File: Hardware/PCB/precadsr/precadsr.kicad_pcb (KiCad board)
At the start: 2 copper layers, 114 x 180 mm, 80 parts, among them J1 AudioJack2_SwitchT, J12 AudioJack2, J13 AudioJack2, J2 Synth_power_2x5, J3 2_pin_Molex_header, J4 Conn_01x10, J5 AudioJack2, J6 Conn_01x04, J7 Conn_01x10, J8 Conn_01x04, J9 2_pin_Molex_connector, Q1 2N3904, Q2 2N3904, Q3 2N3904, U1 ICM7555xP, U2 TL074, U3 LM358

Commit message: Various tweaks
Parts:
- C1, C11: value 1 nF -> 1nF
- C10: value 1 uF -> 1uF
- C2: value 10 nF -> 10nF
- C3: value 10 uF -> 10uF; footprint ao_tht:CP_Radial_D5.0mm_P2.00mm -> ao_tht:CP_Radial_D6.3mm_P2.50mm
- C6, C7, C8, C9: value 100 nF -> 100nF
- moved C3 4.02 mm to (101.6, 27.9), turned to 180 degrees
- moved C10 2.50 mm to (88.9, 27.9), turned to 0 degrees
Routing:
- net SPEED_3: track 7.57 -> 5.16 mm
- net SPEED_1: track 7.30 -> 5.81 mm
- net GATE: track 114.6 -> 113.5 mm
- net THR: track 130.5 -> 131.3 mm

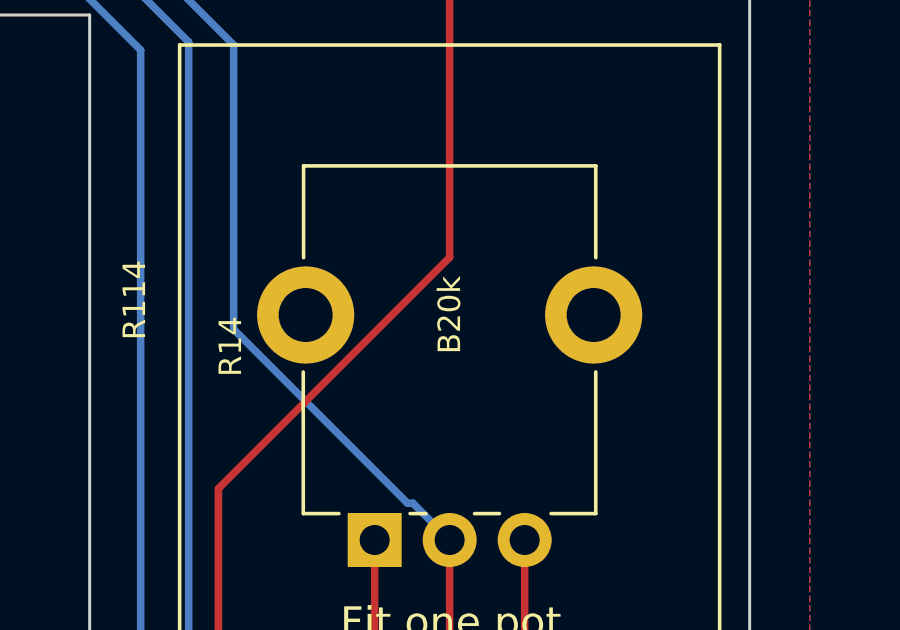
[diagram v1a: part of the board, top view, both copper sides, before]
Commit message: Add comments and graphics symbols to schematics
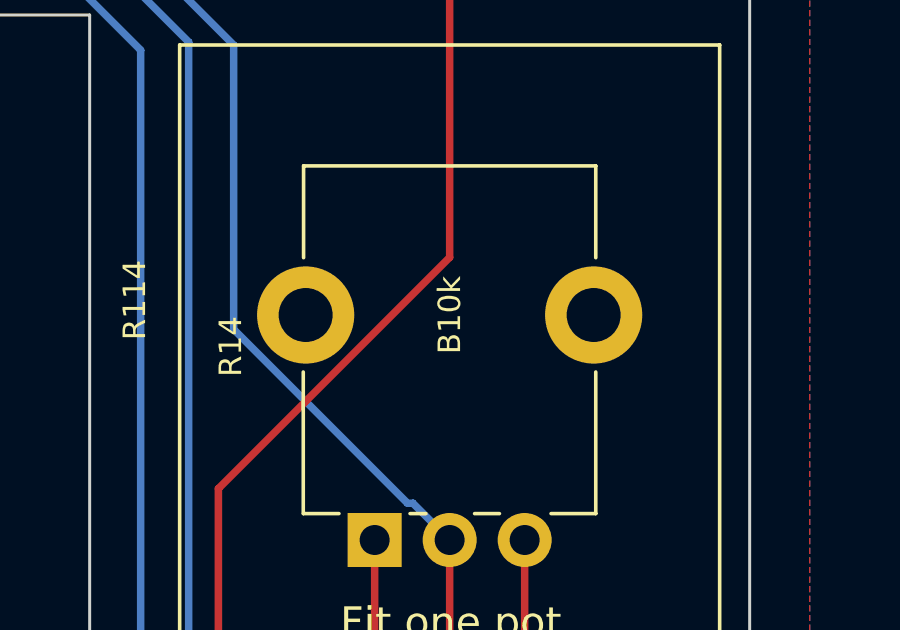
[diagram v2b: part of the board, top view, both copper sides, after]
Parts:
- removed G*** (x2): LOGO, precadsr-panel:precadsr-panel-holes
- added GRAF1: Panel holes, precadsr-panel:precadsr-panel-holes, F.Cu at (38.0, 110.0)
- added GRAF2: Panel holes, precadsr-panel:precadsr-panel-holes, F.Cu at (108.0, 110.0)
- R114, R14: value B20k -> B10k
- R15: value 10k -> 4.7k
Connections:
- net SPEED_2 renamed POTS
- net SPEED_2_P renamed POTS_P

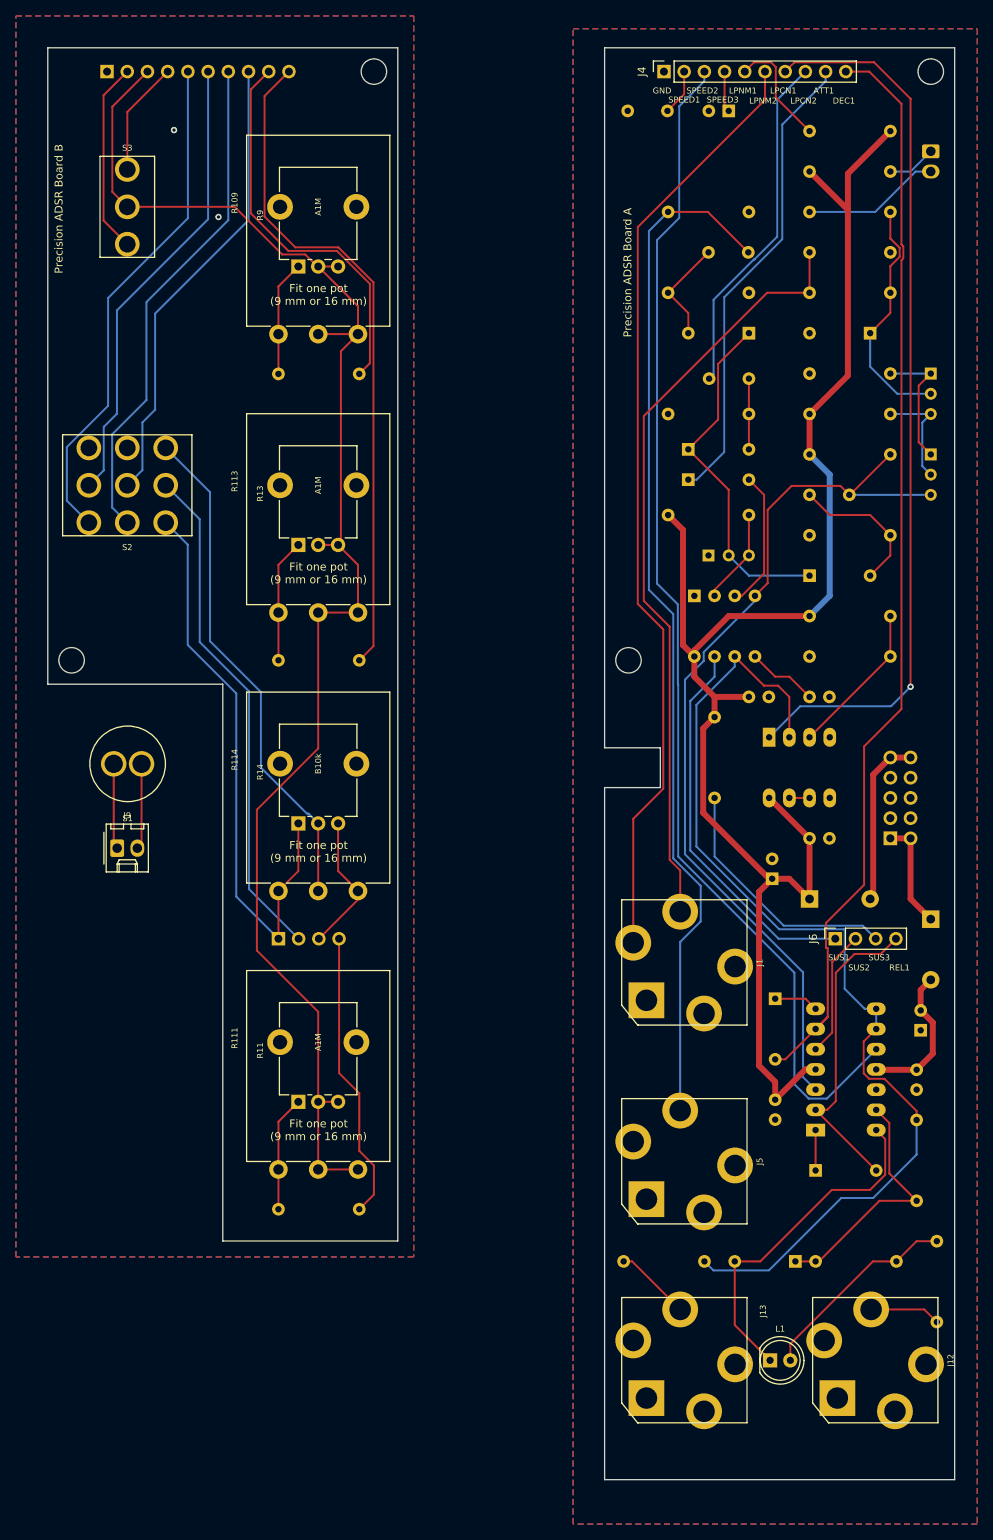
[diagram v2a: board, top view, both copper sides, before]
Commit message: Optional capacitor socket
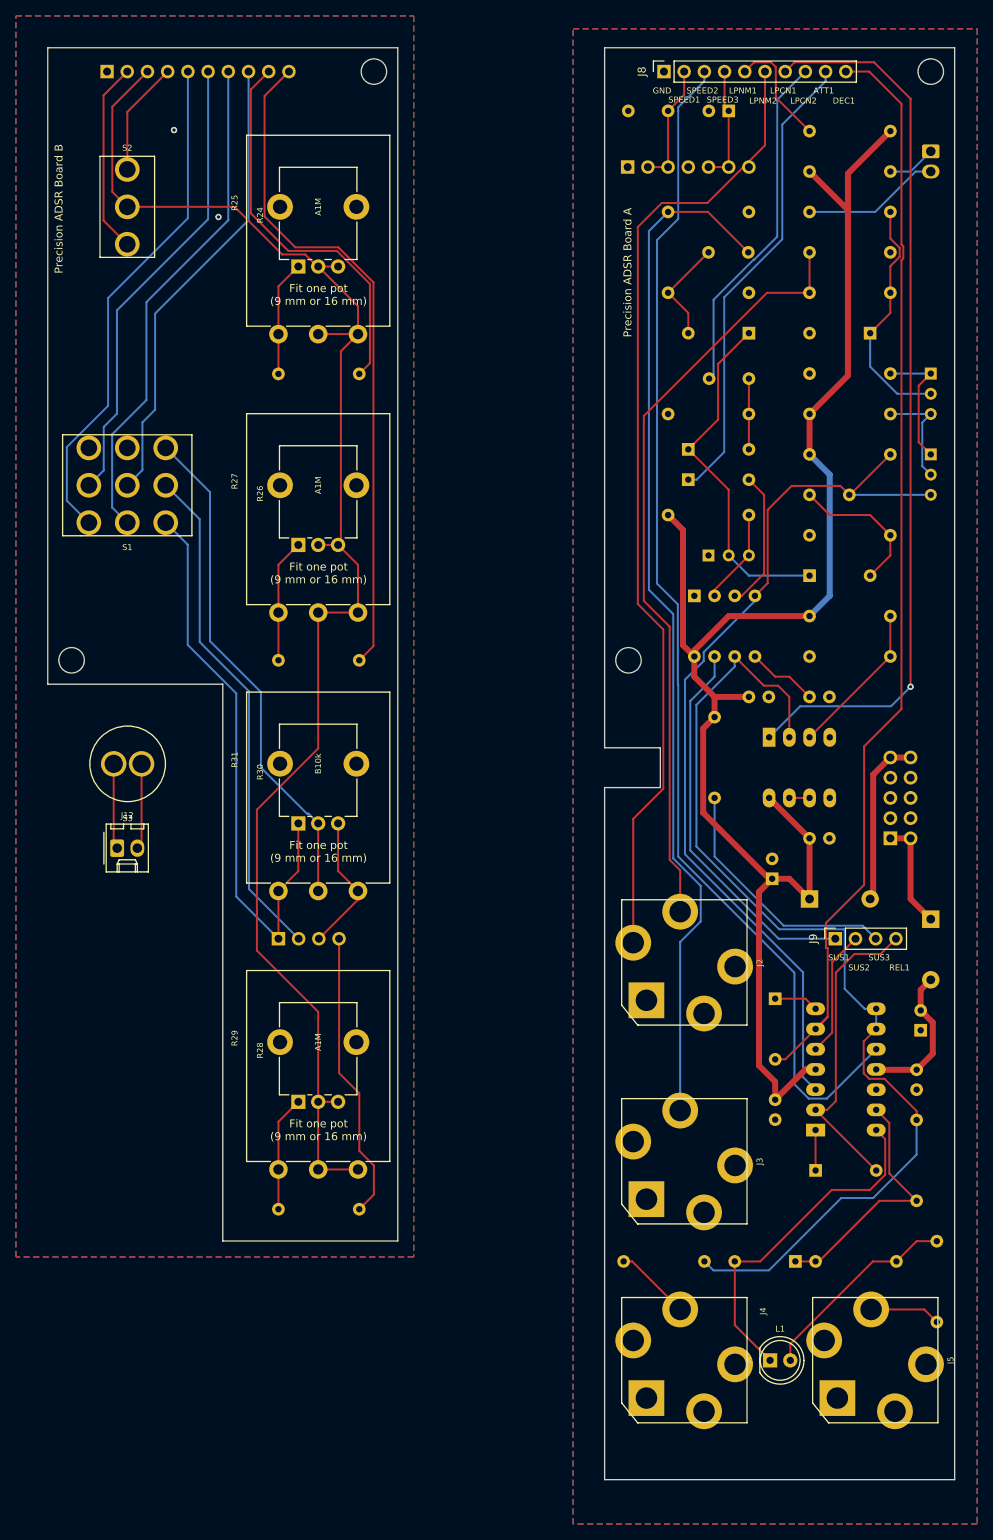
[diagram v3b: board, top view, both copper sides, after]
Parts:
- added J6: Conn_01x07, Connector_PinSocket_2.54mm:PinSocket_1x07_P2.54mm_Vertical, B.Cu at (88.9, 35.0)
- moved C9 0.08 mm to (89.0, 27.9)
- renumbered C2 to C1, C3 to C10, C8 to C2, C5 to C3, C6 to C5, C7 to C6, C1 to C7, C9 to C8, C10 to C9, D6 to D1, D9 to D10, D7 to D2, D1 to D3, D2 to D4, D4 to D5, D3 to D6, D8 to D7, D5 to D8, D10 to D9, J2 to J1, J7 to J10, J8 to J11, J9 to J12, J1 to J2, J5 to J3, J13 to J4, J12 to J5, J3 to J7, J4 to J8, J6 to J9, Q3 to Q1, Q1 to Q2, Q2 to Q3, R7 to R1, R4 to R10, R6 to R11, R17 to R12, R19 to R13, R16 to R14, R18 to R15, R23 to R16, R25 to R17, R26 to R18, R24 to R19, R22 to R2, R27 to R20, R8 to R21, R12 to R22, R10 to R23, R9 to R24, R109 to R25, R13 to R26, R113 to R27, R11 to R28, R111 to R29, R1 to R3, R14 to R30, R114 to R31, R15 to R4, R20 to R5, R21 to R6, R2 to R7, R3 to R8, R5 to R9, S2 to S1, S3 to S2, S1 to S3
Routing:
- net SPEED_3: track 5.16 -> 14.8 mm
- net SPEED_1: track 5.81 -> 15.4 mm
- net LOOP_NORM_2: track 119.0 -> 122.4 mm
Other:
- board text added: "+"
- board text added: "-"

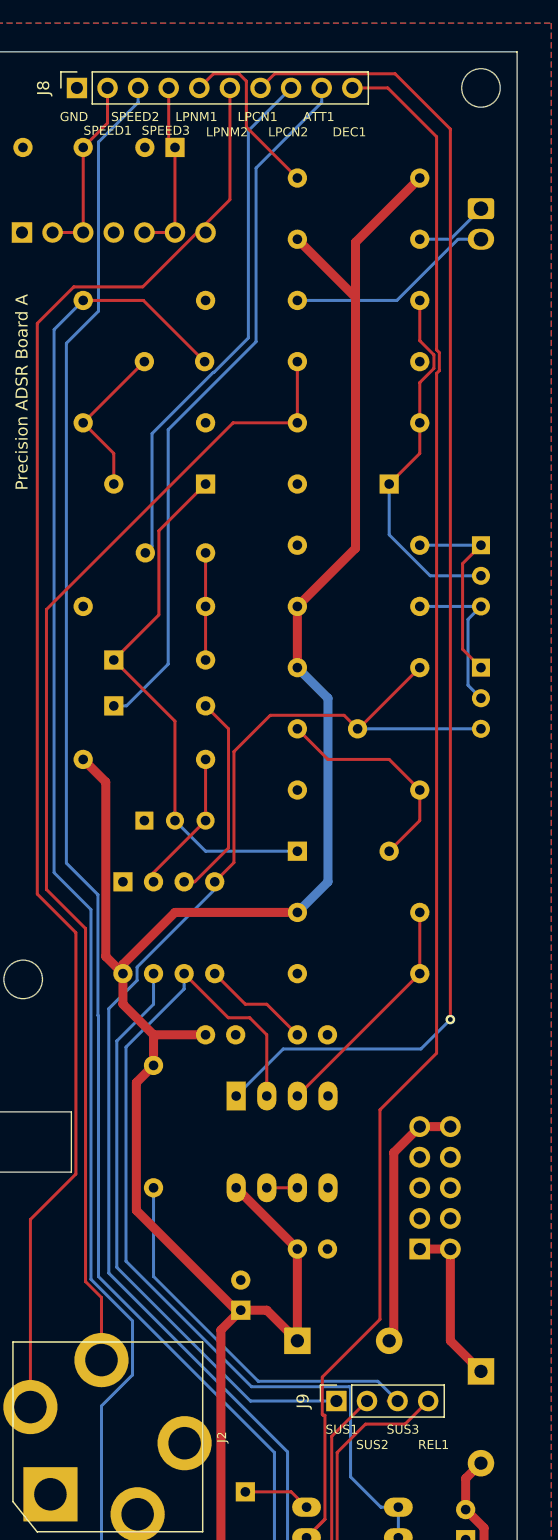
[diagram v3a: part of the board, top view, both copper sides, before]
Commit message: Change op amp, dims to user drawings
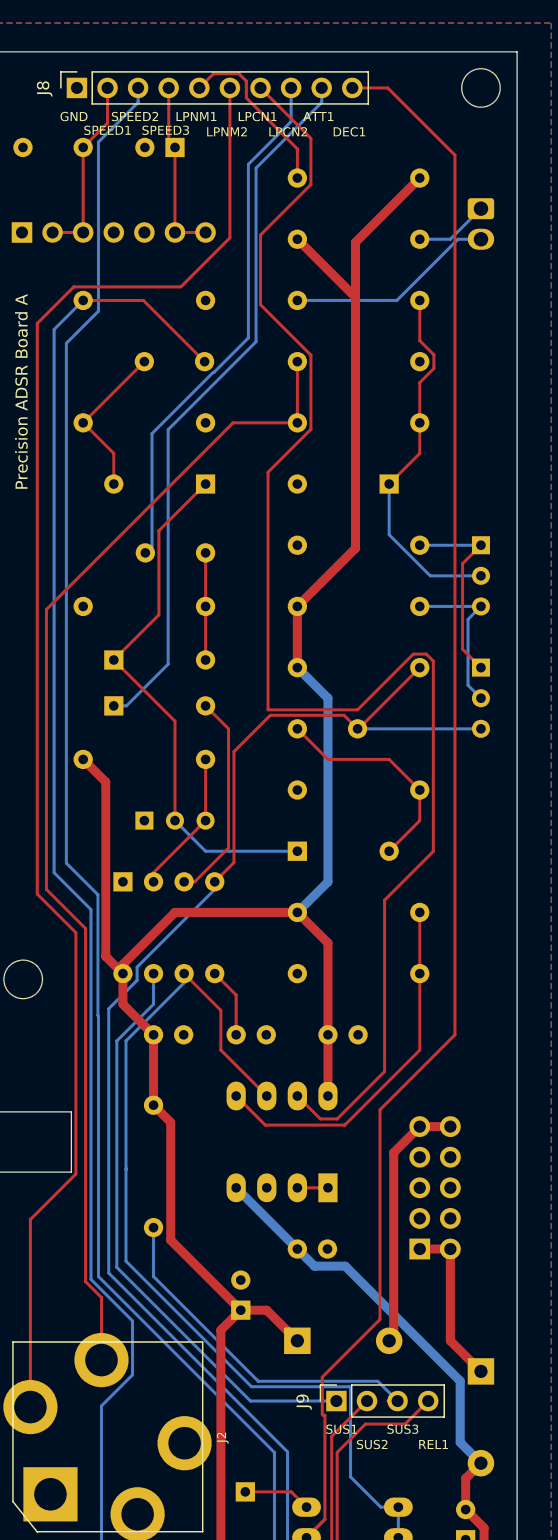
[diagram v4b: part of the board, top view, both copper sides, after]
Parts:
- added C9: 100nF, ao_tht:C_Disc_D3.0mm_W1.6mm_P2.50mm, B.Cu at (114.3, 119.4)
- U3: value LM358 -> TL072
- moved C8 18.0 mm to (114.3, 101.6)
- moved U3 10.8 mm to (114.3, 114.3), turned to 90 degrees
- moved C1 5.08 mm to (106.7, 101.6)
- moved C2 4.32 mm to (99.8, 101.6)
- moved R4 3.30 mm to (99.8, 117.6)
- renumbered C9 to C10, C10 to C11, C11 to C12, C12 to C13
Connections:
- U3 pad 1: LOOP_CONN_1 -> Net-(U3-Pad1)
- U3 pad 2: THR -> Net-(U3-Pad1)
- U3 pad 3: Net-(R17-Pad1) -> GND
- U3 pad 4: GND -> -12V
- U3 pad 5: GND -> Net-(R17-Pad1)
- U3 pad 6: Net-(U3-Pad6) -> THR
- U3 pad 7: Net-(U3-Pad6) -> LOOP_CONN_1
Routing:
- net -12V: track 18.5 -> 51.3 mm
- net Net-(R17-Pad1): track 19.4 -> 30.2 mm
- net LOOP_CONN_1: track 112.5 -> 119.6 mm, vias 1 -> 0
- net +12V: track 204.1 -> 200.3 mm
- net SUS3: track 32.7 -> 29.4 mm
- net Net-(C1-Pad1): track 8.96 -> 5.82 mm
- net Net-(U3-Pad6): track 2.54 -> 0.00 mm
- net Net-(U3-Pad1): track 0.00 -> 2.54 mm
- net LOOP_NORM_2: track 122.4 -> 124.2 mm
- net DEC1: track 138.7 -> 139.8 mm
- net THR: track 131.3 -> 130.4 mm
